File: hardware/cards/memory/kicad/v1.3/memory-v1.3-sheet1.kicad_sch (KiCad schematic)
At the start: 29 parts, among them IC12 74*74, IC3 74*32, X1 FABC96R

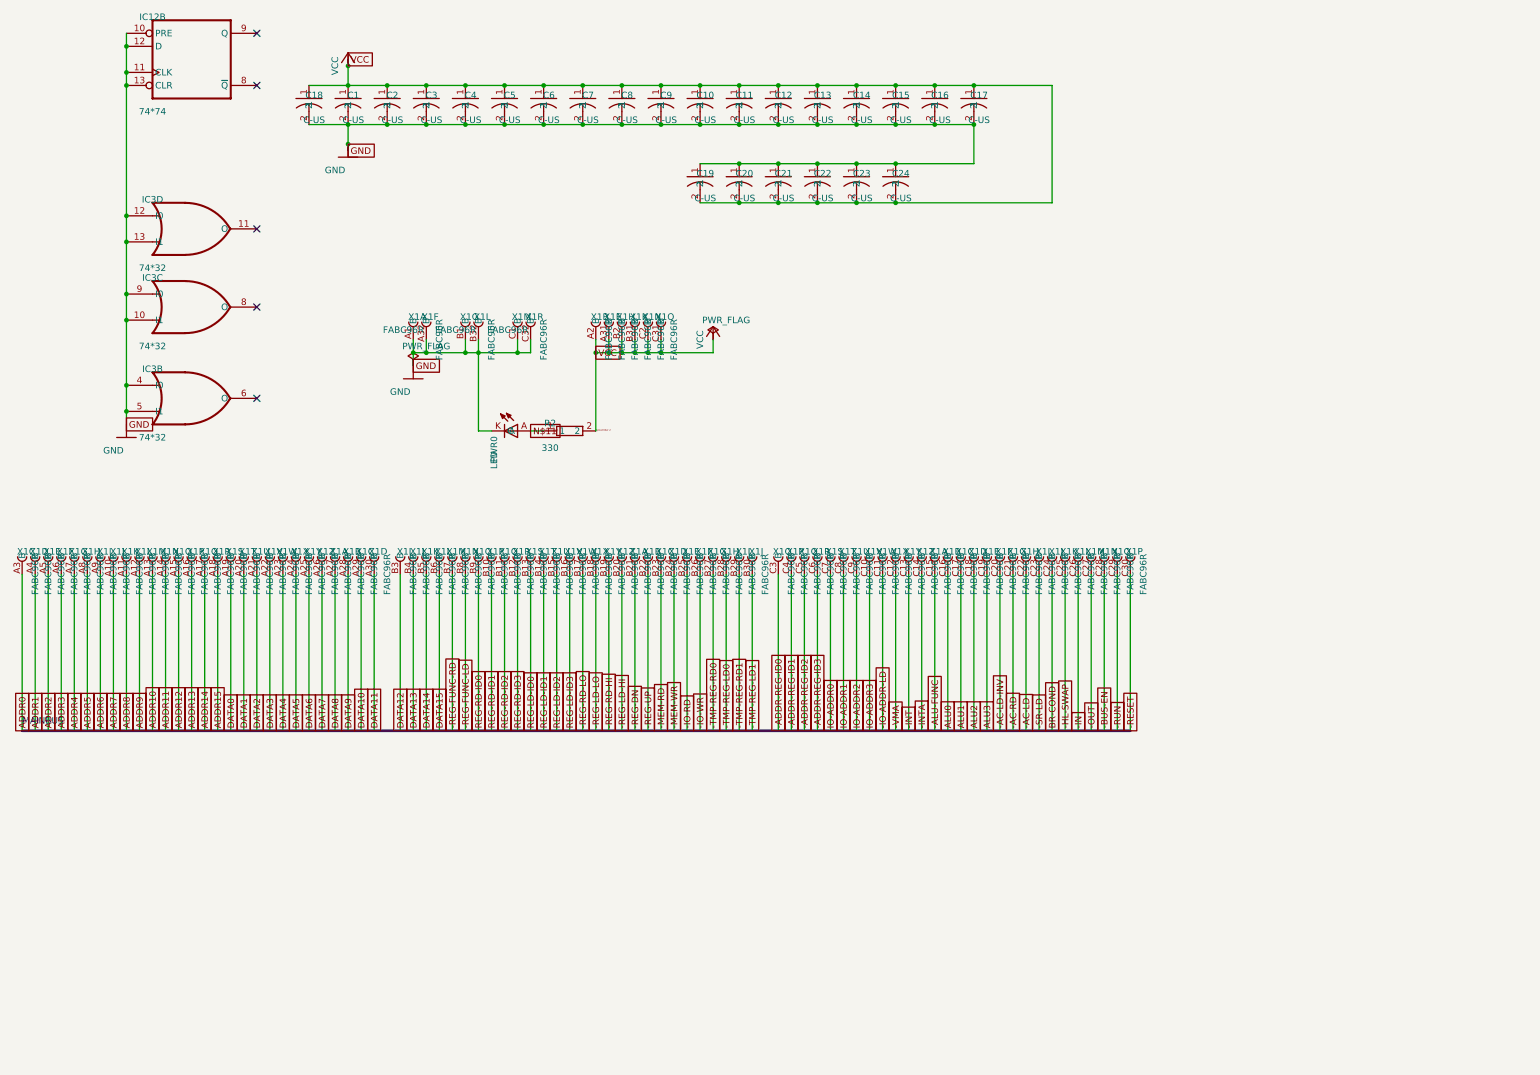
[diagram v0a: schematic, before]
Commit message: fix(kicad): readable converted schematics - overlaps 42,847 -> 3,147, nothing off the frame; CF sheet 0 overlaps
- tools/kicad/sch_overlaps.py: calibrated readability check (text/text, text/body, text/line, off frame/title block)
- eagle_sch_to_kicad.py: fields placed from Eagle's smashed attributes or the symbol's >NAME/>VALUE with Eagle's align,
  size and ratio, readable angles; fields Eagle never shows hidden (FABC96R shows only its pin name); pin numbers hidden
  where every Eagle pin hides them; Eagle-hidden layers dropped (the stray SpiceOrder text); labels on their own wires,
  converter labels only where KiCad needs them; rotate-then-mirror fixed for MR90/MR270 in pin_world/no-connects;
  each sheet on the smallest page that holds it, centred clear of the title block
- finish_board.py: stable footprint-library choice (DRC counts no longer vary run to run)
- all 37 projects regenerated: netlist proofs unchanged (34 MATCH, 2 schematic-only, video Fusion export MISMATCH as
  before); DRC same or better; ERC up (loose wire ends onto graphic buses no longer hidden by labels; explained per README)
- CF card: gate names off the gate bodies, U3 clear of its title, 5.08 mm connector pins; rebuilt: DRC 0/0, proof MATCH
- schematic PDFs regenerated (tools/sch_to_pdf.py, 37/37)

Co-Authored-By: Claude Opus 5.5 <noreply@anthropic.com>
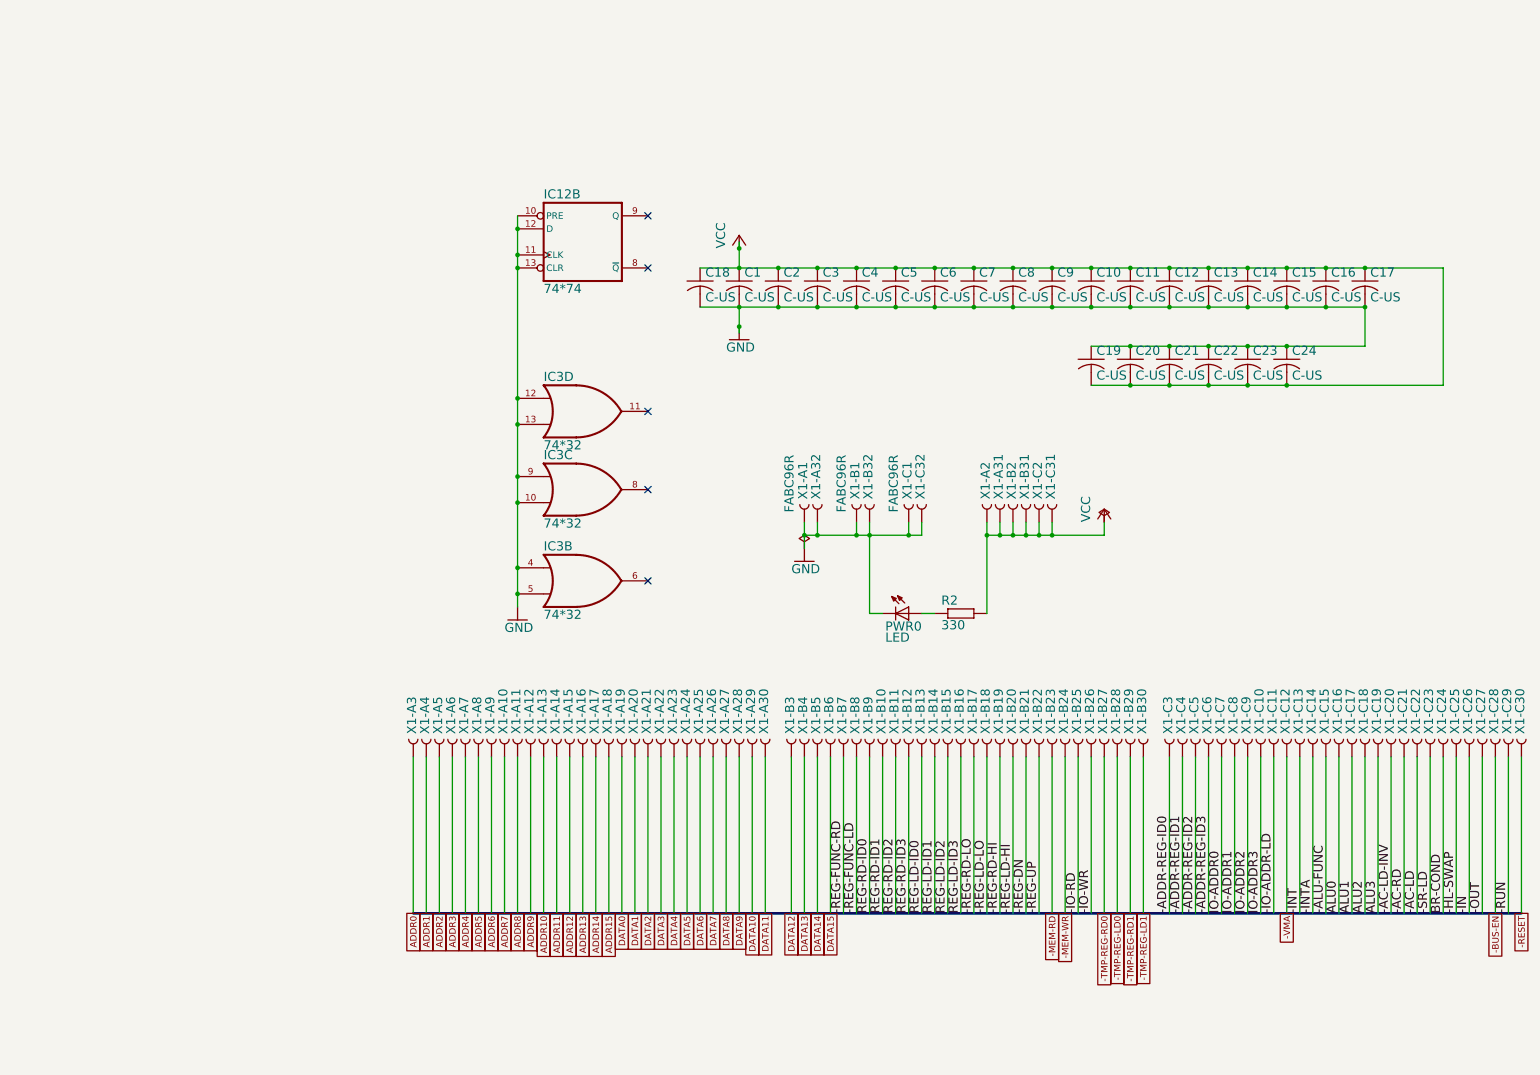
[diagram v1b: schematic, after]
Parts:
- X1: Eagle name (none) -> X1-C21
- X1: Eagle name (none) -> X1-C20
- X1: Eagle name (none) -> X1-C19
- X1: Eagle name (none) -> X1-C23
- X1: Eagle name (none) -> X1-C8
- X1: Eagle name (none) -> X1-A9
- X1: Eagle name (none) -> X1-A27
- X1: Eagle name (none) -> X1-A29
- X1: Eagle name (none) -> X1-C18
- X1: Eagle name (none) -> X1-C25
- X1: Eagle name (none) -> X1-B27
- X1: Eagle name (none) -> X1-B7
- X1: Eagle name (none) -> X1-C14
- X1: Eagle name (none) -> X1-C10
- X1: Eagle name (none) -> X1-B2
- X1: Eagle name (none) -> X1-C28
- X1: Eagle name (none) -> X1-A14
- X1: Eagle name (none) -> X1-A16
- X1: Eagle name (none) -> X1-A11
- X1: Eagle name (none) -> X1-A4
- X1: Eagle name (none) -> X1-A22
- X1: Eagle name (none) -> X1-A26
- X1: Eagle name (none) -> X1-B15
- X1: Eagle name (none) -> X1-C12
- X1: Eagle name (none) -> X1-C6
- X1: Eagle name (none) -> X1-C30
- X1: Eagle name (none) -> X1-B28
- X1: Eagle name (none) -> X1-A2
- X1: Eagle name (none) -> X1-B6
- X1: Eagle name (none) -> X1-C3
- X1: Eagle name (none) -> X1-C26
- X1: Eagle name (none) -> X1-C5
- X1: Eagle name (none) -> X1-B31
- X1: Eagle name (none) -> X1-C24
- X1: Eagle name (none) -> X1-B5
- X1: Eagle name (none) -> X1-B29
- X1: Eagle name (none) -> X1-C22
- X1: Eagle name (none) -> X1-B19
- X1: Eagle name (none) -> X1-A25
- X1: Eagle name (none) -> X1-C16
- X1: Eagle name (none) -> X1-B21
- X1: Eagle name (none) -> X1-A30
- X1: Eagle name (none) -> X1-B25
- X1: Eagle name (none) -> X1-B1
- X1: Eagle name (none) -> X1-A1
- X1: Eagle name (none) -> X1-C17
- X1: Eagle name (none) -> X1-C27
- X1: Eagle name (none) -> X1-B32
- X1: Eagle name (none) -> X1-A31
- X1: Eagle name (none) -> X1-C4
- X1: Eagle name (none) -> X1-B11
- X1: Eagle name (none) -> X1-B17
- X1: Eagle name (none) -> X1-B10
- X1: Eagle name (none) -> X1-A21
- X1: Eagle name (none) -> X1-C1
- X1: Eagle name (none) -> X1-B30
- X1: Eagle name (none) -> X1-A24
- X1: Eagle name (none) -> X1-B8
- X1: Eagle name (none) -> X1-B14
- X1: Eagle name (none) -> X1-A12
- X1: Eagle name (none) -> X1-A7
- X1: Eagle name (none) -> X1-B22
- X1: Eagle name (none) -> X1-A17
- X1: Eagle name (none) -> X1-B23
- X1: Eagle name (none) -> X1-B16
- X1: Eagle name (none) -> X1-B9
- X1: Eagle name (none) -> X1-C7
- X1: Eagle name (none) -> X1-C11
- X1: Eagle name (none) -> X1-B26
- X1: Eagle name (none) -> X1-A15
- X1: Eagle name (none) -> X1-C9
- X1: Eagle name (none) -> X1-A8
- X1: Eagle name (none) -> X1-A19
- X1: Eagle name (none) -> X1-A20
- X1: Eagle name (none) -> X1-B12
- X1: Eagle name (none) -> X1-B13
- X1: Eagle name (none) -> X1-B20
- X1: Eagle name (none) -> X1-C15
- X1: Eagle name (none) -> X1-C13
- X1: Eagle name (none) -> X1-C2
- X1: Eagle name (none) -> X1-A10
- X1: Eagle name (none) -> X1-A6
- X1: Eagle name (none) -> X1-B24
- X1: Eagle name (none) -> X1-A28
- X1: Eagle name (none) -> X1-B18
- X1: Eagle name (none) -> X1-A13
- X1: Eagle name (none) -> X1-A5
- X1: Eagle name (none) -> X1-C32
- X1: Eagle name (none) -> X1-A3
- X1: Eagle name (none) -> X1-A23
- X1: Eagle name (none) -> X1-C31
- X1: Eagle name (none) -> X1-B3
- X1: Eagle name (none) -> X1-A18
- X1: Eagle name (none) -> X1-B4
- X1: Eagle name (none) -> X1-C29
- X1: Eagle name (none) -> X1-A32
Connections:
- net N$11: no longer names the net of PWR0.A, R2.1
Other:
- note removed: "MAINBUS"
- moved on the sheet: IC12B

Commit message: refactor(memory): built card is eagle/v1.3; the earlier save is eagle/deprecated/v1.3-do-not-use
Ken 2026-09-24: the memory card folders are renamed so the plain v1.3 name is the card in the machine.

- eagle/v1.3/ (earlier save, notes 2025-03-06, board 2021-03-17, NOT the built card) -> eagle/deprecated/v1.3-do-not-use/
  (git mv, contents untouched); its KiCad conversion regenerated as kicad/deprecated/v1.3-do-not-use/ (project
  memory-v1.3-do-not-use, proof MATCH 115/115, still "never fabricated").
- eagle/v1.3-fusion-export-2026-09-24/ (the BUILT card: Ken's Fusion 360 export of 2026-09-24, verified against JLCPCB
  order 2000765A) -> eagle/v1.3/; its conversion regenerated as kicad/v1.3/ (memory-v1.3.*, proof MATCH 116/116).
  verify_fab_vs_brd.py: PASS on eagle/v1.3 (all 695 holes, 1,263 tracks, parts, PnP; gerber set byte-identical to
  the one kept in the deprecated folder), FAIL on the deprecated board as before.
- Migration plan: tools/migrate_dryrun.py sends GV "Memory v1.3" to eagle/deprecated/v1.3-do-not-use/; migration/
  reports re-run (the 30 plan rows differ only by that destination). audit_tree.py: the Fusion-export rule now
  matches eagle/v1.3/ and is checked before the 2026-09-20 run log (which lists the earlier save at that path).
  Audit: 0 unexplained, 0 hash mismatches, 0 plan rows missing.
- fabricated.py -> FABRICATED.md + marker, gen_bom.py (+ docs/bom rows, --check up to date), PROVENANCE.md
  regenerated, KICAD.md rows (stale fusion-export row removed), BOARDS.md/SCHEMATICS.md rows, the memory section of
  DESIGN-REVIEW.md (now the built card: 53 parts, 169 nets, 21 ICs; the rest of that file is left at its 09-21 run).
- memory v2.0 reads ../v1.3: BASE_NAME/BASE/space_check path/docstrings/MASTER/README. The copied library is renamed
  memory-v1.3-eagle (the regenerated base's nickname; gen_mem_v2.py sch copies it with the lib tables). The converter
  derives schematic UUIDs from the project name, so in the boards a NOROUTE build does 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
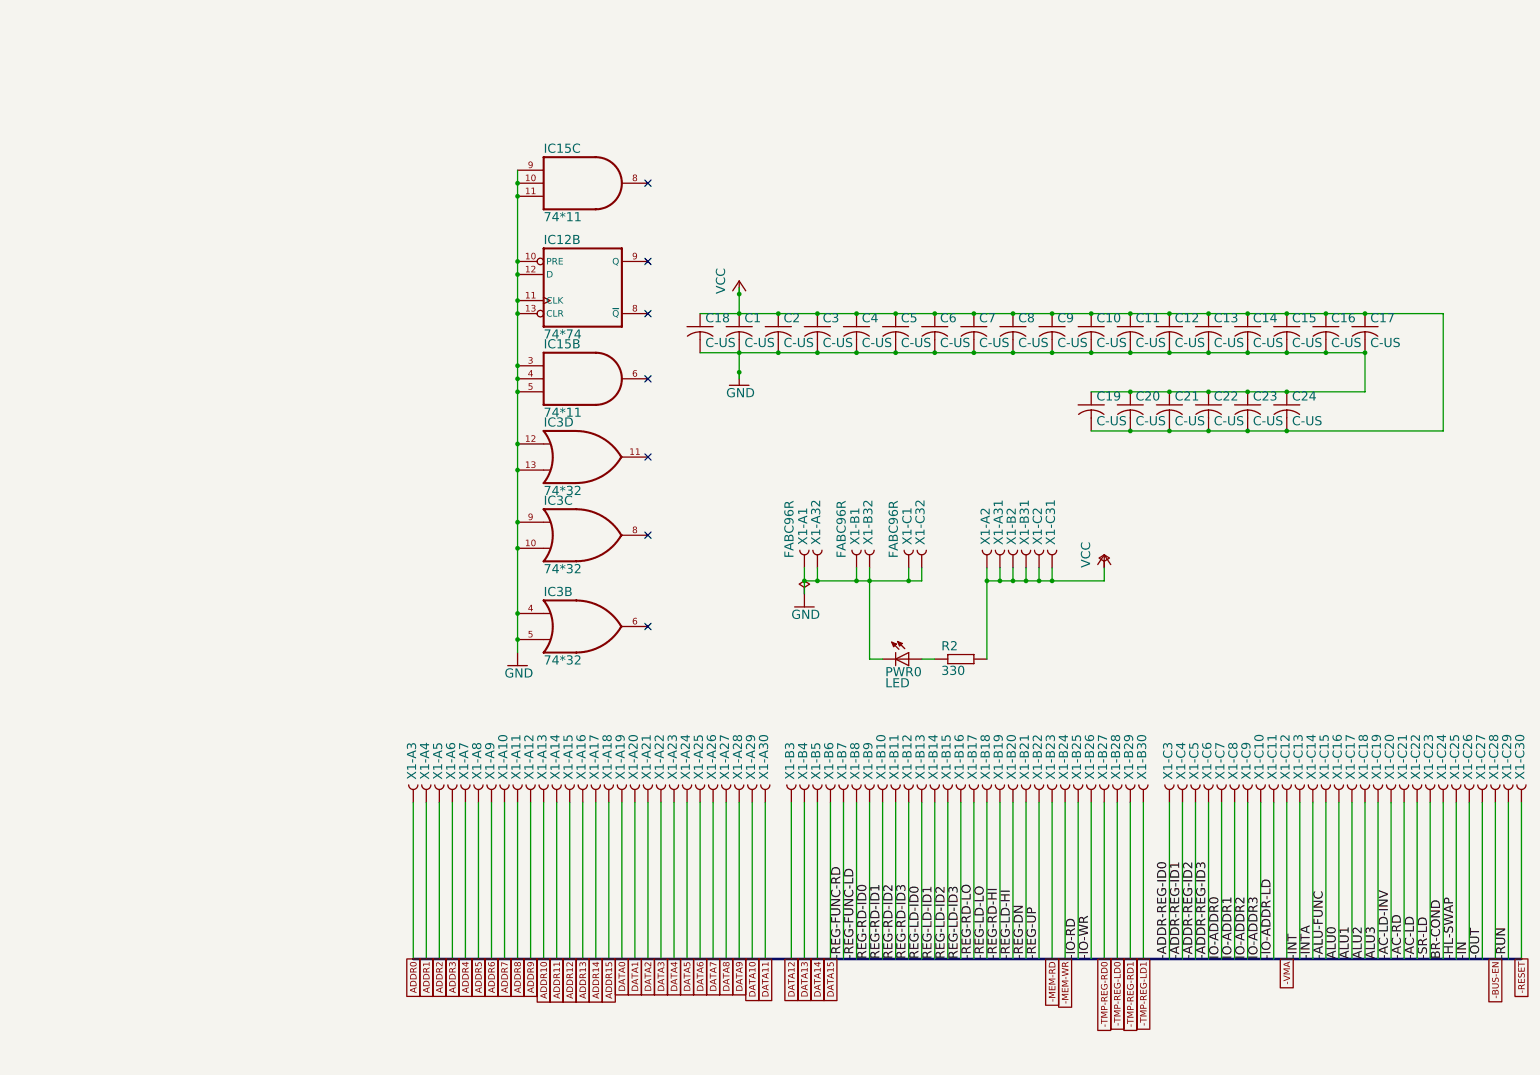
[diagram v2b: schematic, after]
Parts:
- added IC15: 74*11, memory-v1.3-eagle:DIL14, symbol memory-v1.3-eagle:74xx-us_74x11_N_pwrhidden
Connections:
- net GND: now also IC15.10 (I1), IC15.11 (I2), IC15.3 (I0), IC15.4 (I1), IC15.5 (I2), IC15.7 (GND), IC15.7 (GND), IC15.9 (I0)
- net VCC: now also IC15.14 (VCC), IC15.14 (VCC)
- no-connect marks 5 -> 7
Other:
- moved on the sheet: C1, C10, C11, C12, C13, C14, C15, C16, C17, C18, C19, C2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
